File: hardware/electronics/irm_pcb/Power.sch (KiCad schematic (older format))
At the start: 4 parts, among them J16 Screw_Terminal_01x02, U6 LM1117-3.3, U7 TSR1-2450

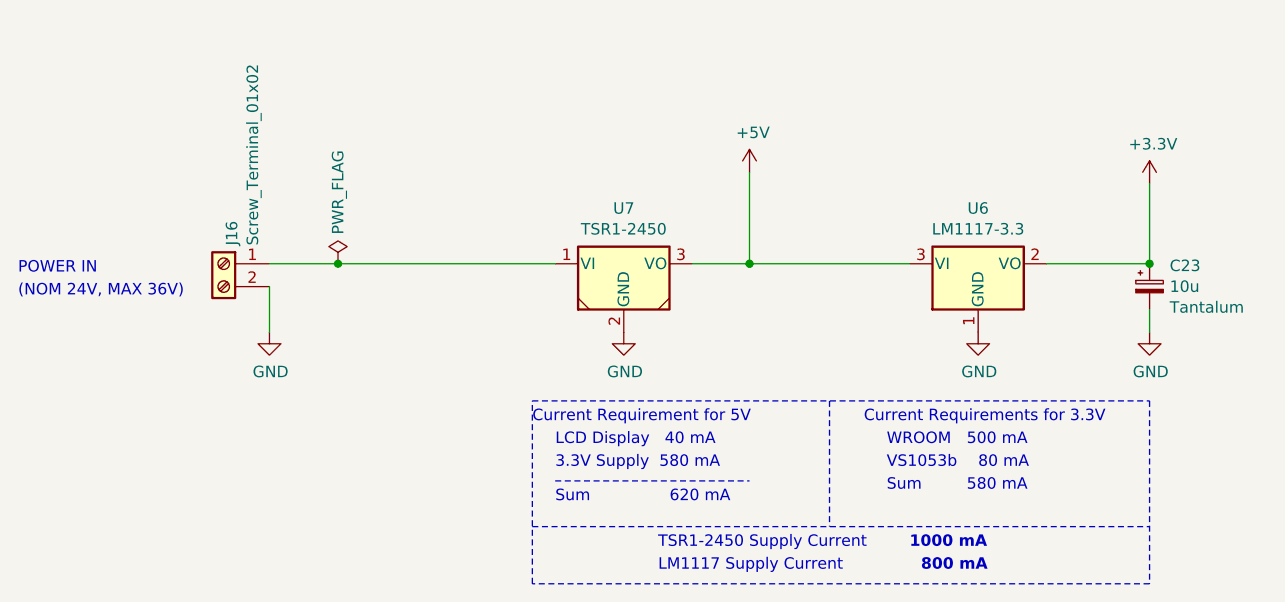
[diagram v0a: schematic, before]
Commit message: New borad layout - routing incomplete
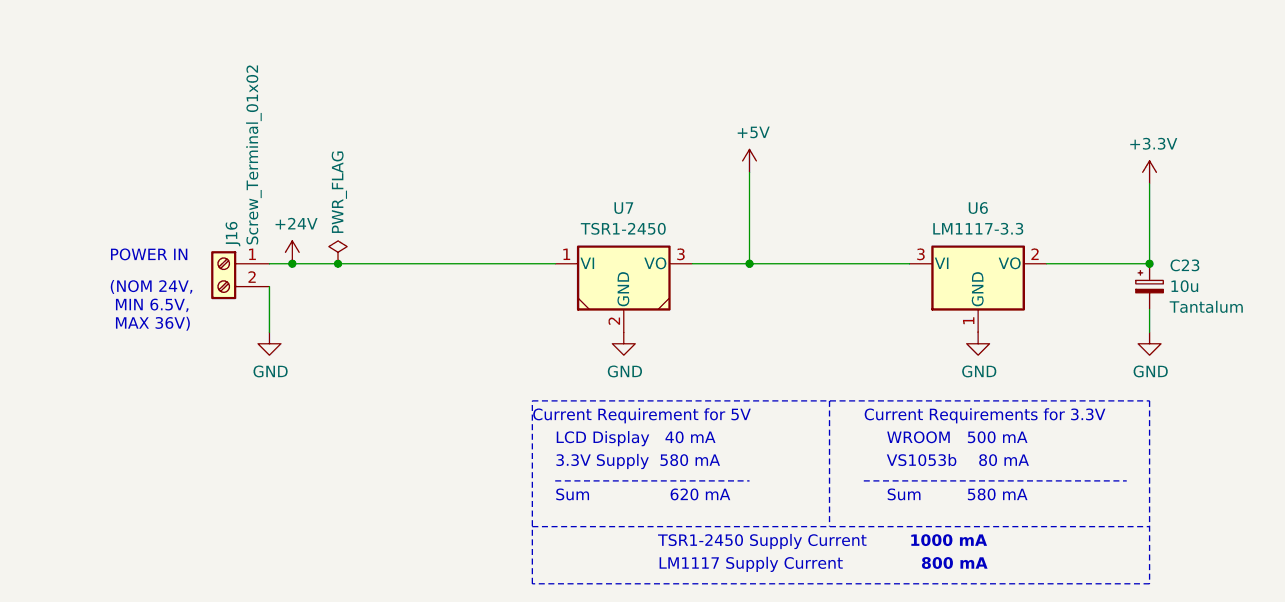
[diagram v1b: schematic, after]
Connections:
- net +24V: now reaches J16.1 (Pin_1), U7.1 (VI)
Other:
- note added: "(NOM 24V, \n MIN 6.5V, \n MAX 36V)"
- note removed: "(NOM 24V, MAX 36V)"
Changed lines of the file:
@@
 Wire Wire Line
 	7700 4450 7700 4550
-Text Notes 2750 4300 0    50   ~ 0
+Text Notes 3150 4250 0    50   ~ 0
 POWER IN
 $Comp
@@
 Text Notes 6950 5150 0    50   ~ 0
 80 mA
-Text Notes 6550 5250 0    50   ~ 0
+Text Notes 6550 5300 0    50   ~ 0
 Sum
-Text Notes 6900 5250 0    50   ~ 0
+Text Notes 6900 5300 0    50   ~ 0
 580 mA
 Text Notes 6700 5600 0    50   ~ 10
@@
 	1    0    0    -1
 $EndComp
-Text Notes 2750 4400 0    50   ~ 0
-(NOM 24V, MAX 36V)
+Text Notes 3150 4550 0    50   ~ 0
+(NOM 24V, \n MIN 6.5V, \n MAX 36V)
 $Comp
 L modular-internet-radio:TSR1-2450 U7
@@
 	6300 4850 6300 5400
 Wire Wire Line
-	3850 4250 4150 4250
+	3850 4250 3950 4250
 Connection ~ 4150 4250
 Wire Wire Line
 	4150 4250 5100 4250
+Wire Notes Line
+	6450 5200 7600 5200
+$Comp
+L power:+24V #PWR0105
+U 1 1 5DE7C86F
+P 3950 4250
+F 0 "#PWR0105" H 3950 4100 50  0001 C CNN
+F 1 "+24V" H 3965 4423 50  0000 C CNN
+F 2 "" H 3950 4250 50  0001 C CNN
+F 3 "" H 3950 4250 50  0001 C CNN
+	1    3950 4250
+	1    0    0    -1
+$EndComp
+Connection ~ 3950 4250
+Wire Wire Line
+	3950 4250 4150 4250
 $EndSCHEMATC
